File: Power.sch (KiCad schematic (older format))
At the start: 22 parts, among them U2 MCP1700T-3302E/TT_

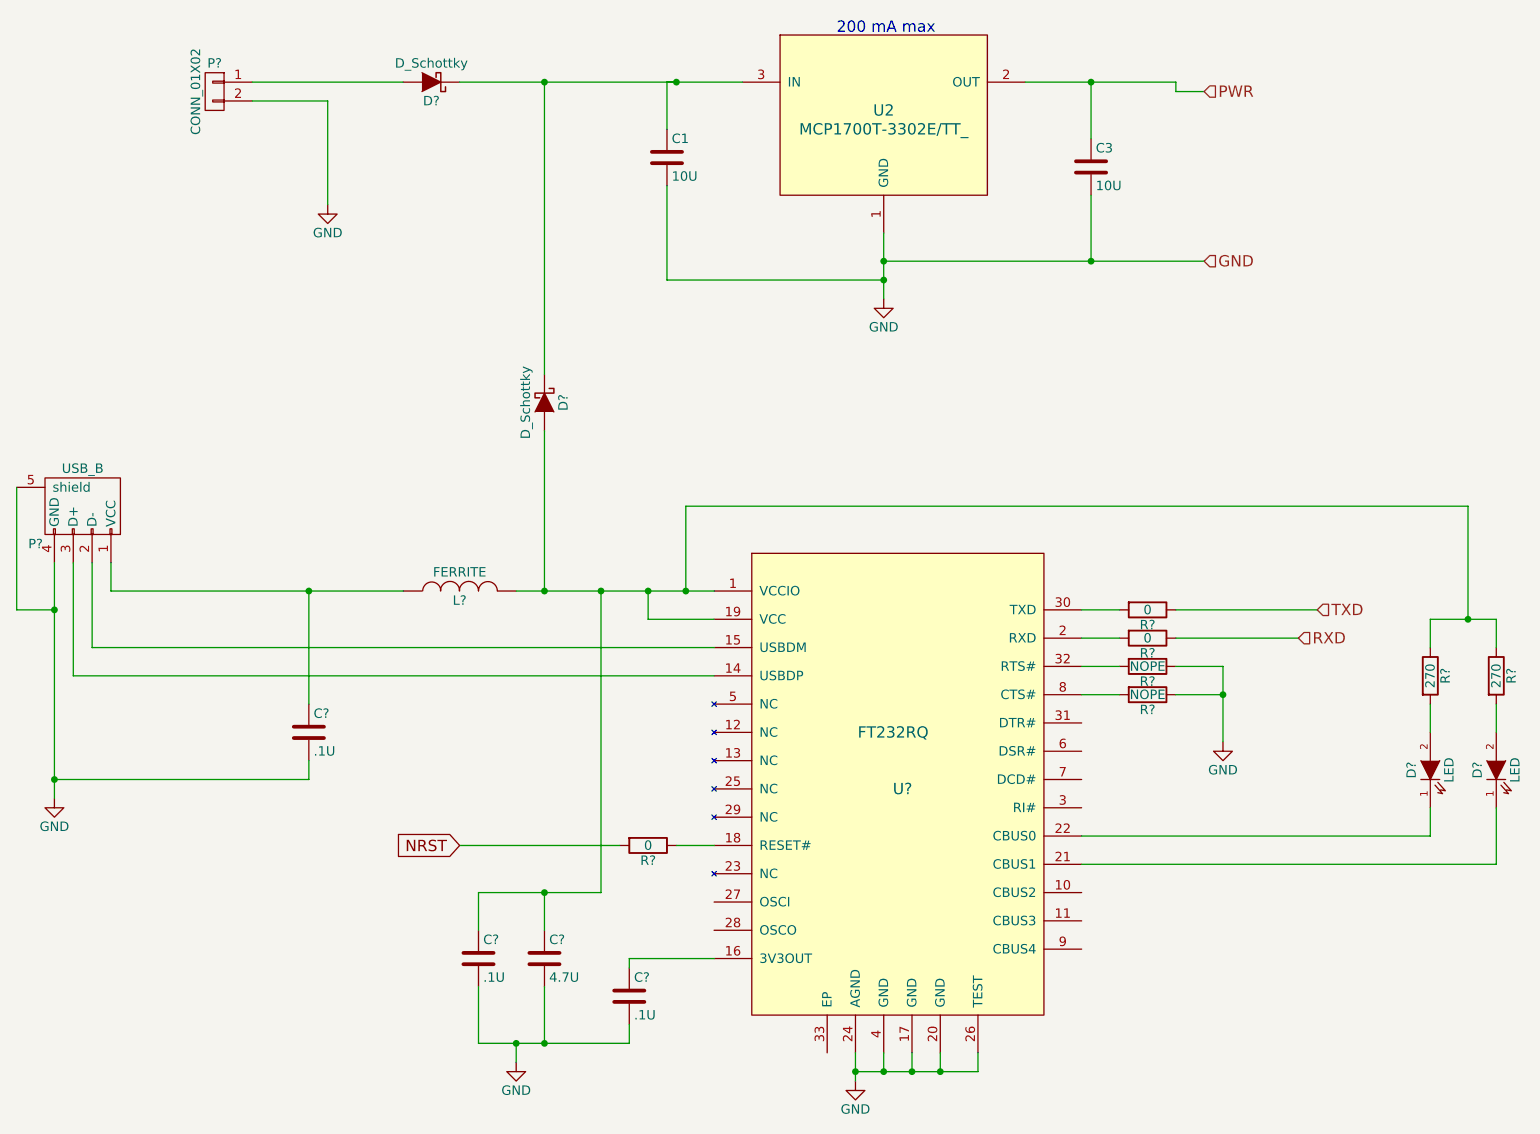
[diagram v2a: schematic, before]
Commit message: Associated footprints, created footprints for 2mm connector and did prelim placement
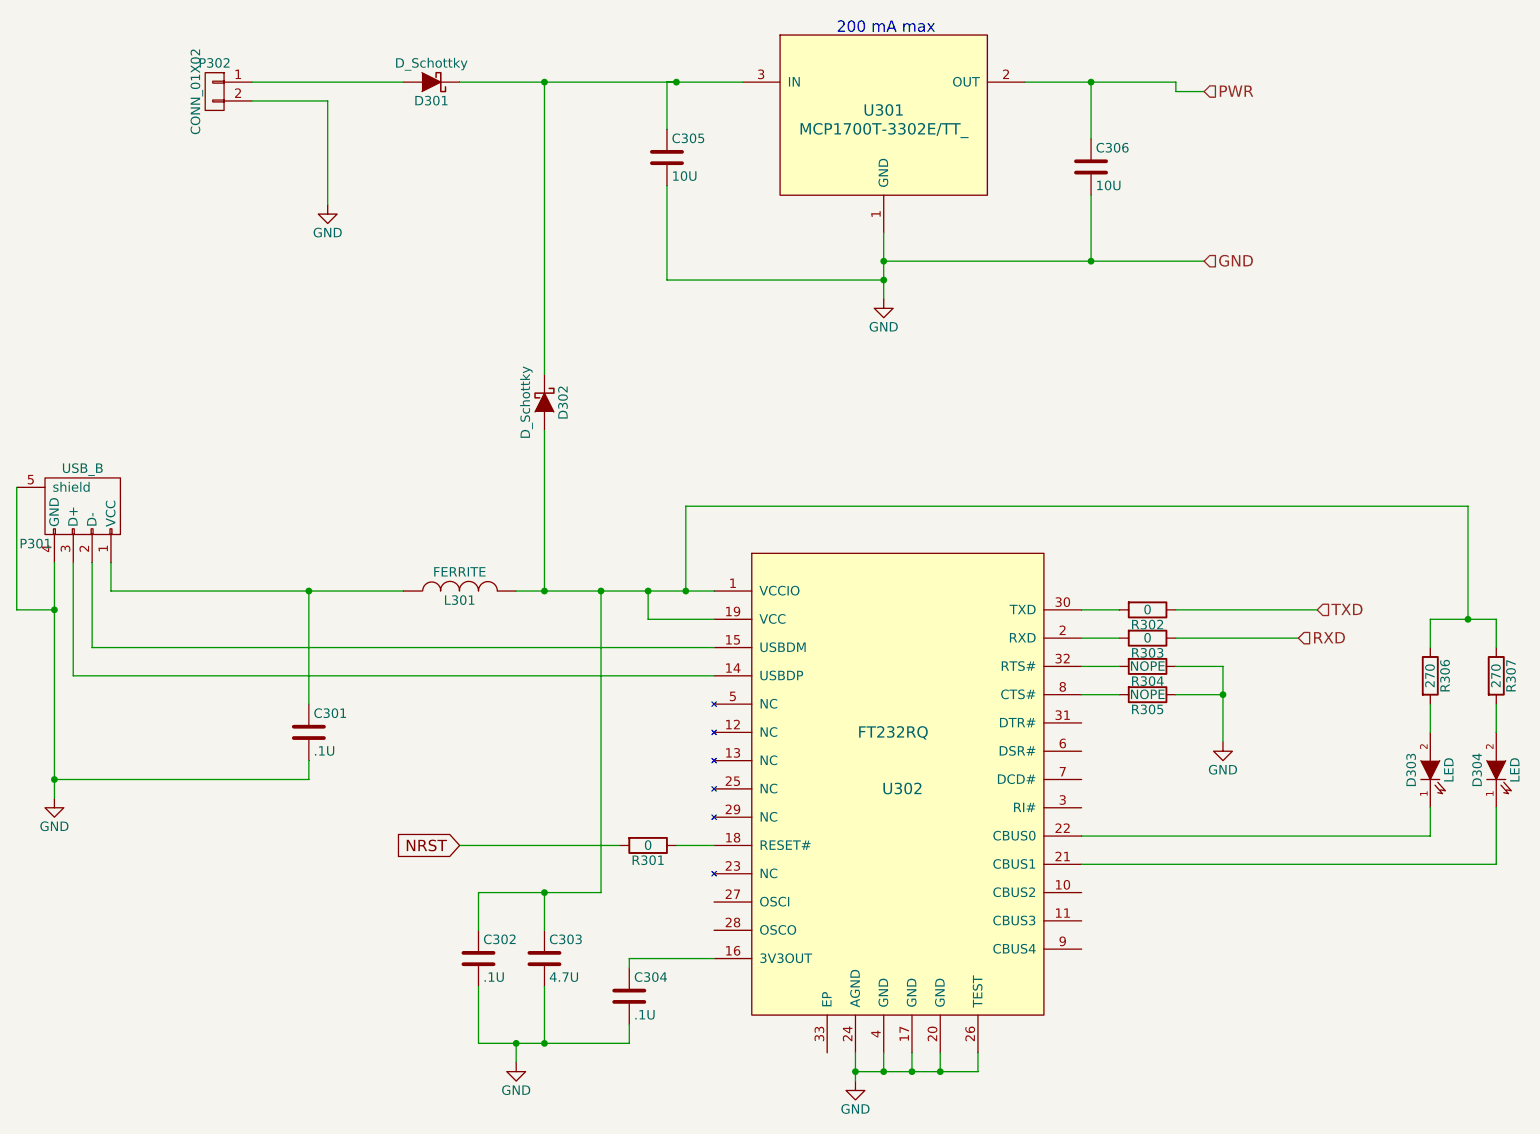
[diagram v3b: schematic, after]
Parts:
- C301, C302, C304: renamed from C?; footprint (none) -> Capacitors_SMD:C_0805
- C303: renamed from C?; footprint (none) -> Capacitors_SMD:C_1210
- C305: renamed from C1; footprint Capacitors_SMD:C_0805 -> Capacitors_SMD:C_1210
- C306: renamed from C3; footprint Capacitors_SMD:C_0805 -> Capacitors_SMD:C_1210
- D301, D302: renamed from D?; footprint (none) -> Diodes_SMD:Diode-SMA_Standard
- D303, D304: renamed from D?; footprint (none) -> LEDs:LED-0805
- L301: renamed from L?; footprint (none) -> Inductors_NEOSID:Neosid_Inductor_SM1206
- P301: renamed from P?; footprint (none) -> CentralCommand:10118193
- P302: renamed from P?; footprint (none) -> Pin_Headers:Pin_Header_Straight_1x02
- R301, R302, R303, R304, R305, R306, R307: renamed from R?; footprint (none) -> Resistors_SMD:R_0805
- U302: renamed from U?; footprint (none) -> Housings_DFN_QFN:QFN-32-1EP_5x5mm_Pitch0.5mm
- renumbered U2 to U301
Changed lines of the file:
@@
 $Descr A4 11693 8268
 encoding utf-8
-Sheet 2 3
+Sheet 3 3
 Title ""
 Date ""
@@
 $EndDescr
 $Comp
-L MCP1700T-3302E/TT_ U2
+L MCP1700T-3302E/TT_ U301
 U 1 1 56441A93
 P 5500 1100
-F 0 "U2" H 5500 1100 60  0000 C CNN
+F 0 "U301" H 5500 1100 60  0000 C CNN
 F 1 "MCP1700T-3302E/TT_" H 5500 1000 60  0000 C CNN
 F 2 "Housings_SOT-23_SOT-143_TSOT-6:SOT-23" H 5500 1100 60  0001 C CNN
@@
 $EndComp
 $Comp
-L C C1
+L C C305
 U 1 1 56441A9A
 P 4350 1350
-F 0 "C1" H 4375 1450 50  0000 L CNN
+F 0 "C305" H 4375 1450 50  0000 L CNN
 F 1 "10U" H 4375 1250 50  0000 L CNN
-F 2 "Capacitors_SMD:C_0805" H 4388 1200 30  0001 C CNN
+F 2 "Capacitors_SMD:C_1210" H 4388 1200 30  0001 C CNN
 F 3 "" H 4350 1350 60  0000 C CNN
 	1    4350 1350
@@
 $EndComp
 $Comp
-L C C3
+L C C306
 U 1 1 56441AA1
 P 6600 1400
-F 0 "C3" H 6625 1500 50  0000 L CNN
+F 0 "C306" H 6625 1500 50  0000 L CNN
 F 1 "10U" H 6625 1300 50  0000 L CNN
-F 2 "Capacitors_SMD:C_0805" H 6638 1250 30  0001 C CNN
+F 2 "Capacitors_SMD:C_1210" H 6638 1250 30  0001 C CNN
 F 3 "" H 6600 1400 60  0000 C CNN
 	1    6600 1400
@@
 $EndComp
 $Comp
-L GND #PWR?
+L GND #PWR08
 U 1 1 56441AA8
 P 5500 2100
-F 0 "#PWR?" H 5500 1850 50  0001 C CNN
+F 0 "#PWR08" H 5500 1850 50  0001 C CNN
 F 1 "GND" H 5500 1950 50  0000 C CNN
 F 2 "" H 5500 2100 60  0000 C CNN
@@
 200 mA max
 $Comp
-L CONN_01X02 P?
+L CONN_01X02 P302
 U 1 1 56442D62
 P 1950 1000
-F 0 "P?" H 1950 1150 50  0000 C CNN
+F 0 "P302" H 1950 1150 50  0000 C CNN
 F 1 "CONN_01X02" V 2050 1000 50  0000 C CNN
-F 2 "" H 1950 1000 60  0000 C CNN
+F 2 "Pin_Headers:Pin_Header_Straight_1x02" H 1950 1000 60  0001 C CNN
 F 3 "" H 1950 1000 60  0000 C CNN
 	1    1950 1000
@@
 $EndComp
 $Comp
-L GND #PWR?
+L GND #PWR09
 U 1 1 56442E32
 P 2550 1600
-F 0 "#PWR?" H 2550 1350 50  0001 C CNN
+F 0 "#PWR09" H 2550 1350 50  0001 C CNN
 F 1 "GND" H 2550 1450 50  0000 C CNN
 F 2 "" H 2550 1600 60  0000 C CNN
@@
 $EndComp
 $Comp
-L FT232RQ U?
+L FT232RQ U302
 U 1 1 565601D9
 P 5550 4750
-F 0 "U?" H 5600 4800 60  0000 C CNN
+F 0 "U302" H 5600 4800 60  0000 C CNN
 F 1 "FT232RQ" H 5550 5100 60  0000 C CNN
-F 2 "" H 7700 4900 60  0000 C CNN
+F 2 "Housings_DFN_QFN:QFN-32-1EP_5x5mm_Pitch0.5mm" H 7700 4900 60  0001 C CNN
 F 3 "" H 7700 4900 60  0000 C CNN
 	1    5550 4750
@@
 $EndComp
 $Comp
-L USB_B P?
+L USB_B P301
 U 1 1 56560CE5
 P 1200 3200
-F 0 "P?" H 1400 3000 50  0000 C CNN
+F 0 "P301" H 1400 3000 50  0000 C CNN
 F 1 "USB_B" H 1150 3400 50  0000 C CNN
-F 2 "" V 1150 3100 60  0000 C CNN
+F 2 "CentralCommand:10118193" V 1150 3100 60  0001 C CNN
 F 3 "" V 1150 3100 60  0000 C CNN
 	1    1200 3200
@@
 	2550 1050 2550 1600
 $Comp
-L INDUCTOR L?
+L INDUCTOR L301
 U 1 1 56560EFA
 P 3250 3650
-F 0 "L?" V 3200 3650 50  0000 C CNN
+F 0 "L301" V 3200 3650 50  0000 C CNN
 F 1 "FERRITE" V 3350 3650 50  0000 C CNN
-F 2 "" H 3250 3650 60  0000 C CNN
+F 2 "Inductors_NEOSID:Neosid_Inductor_SM1206" H 3250 3650 60  0001 C CNN
 F 3 "" H 3250 3650 60  0000 C CNN
 	1    3250 3650
@@
 	1400 3650 2950 3650
 $Comp
-L C C?
+L C C301
 U 1 1 565612DF
 P 2450 4400
-F 0 "C?" H 2475 4500 50  0000 L CNN
+F 0 "C301" H 2475 4500 50  0000 L CNN
 F 1 ".1U" H 2475 4300 50  0000 L CNN
-F 2 "" H 2488 4250 30  0000 C CNN
+F 2 "Capacitors_SMD:C_0805" H 2488 4250 30  0001 C CNN
 F 3 "" H 2450 4400 60  0000 C CNN
 	1    2450 4400
@@
 	1100 3500 1100 4750
 $Comp
-L GND #PWR?
+L GND #PWR010
 U 1 1 565615CA
 P 1100 4750
-F 0 "#PWR?" H 1100 4500 50  0001 C CNN
+F 0 "#PWR010" H 1100 4500 50  0001 C CNN
 F 1 "GND" H 1100 4600 50  0000 C CNN
 F 2 "" H 1100 4750 60  0000 C CNN
@@
 RXD
 $Comp
-L D_Schottky D?
+L D_Schottky D301
 U 1 1 565622B8
 P 3100 950
-F 0 "D?" H 3100 1050 50  0000 C CNN
+F 0 "D301" H 3100 1050 50  0000 C CNN
 F 1 "D_Schottky" H 3100 850 50  0000 C CNN
-F 2 "" H 3100 950 60  0000 C CNN
+F 2 "Diodes_SMD:Diode-SMA_Standard" H 3100 950 60  0001 C CNN
 F 3 "" H 3100 950 60  0000 C CNN
 	1    3100 950
@@
 	2950 950  2150 950
 $Comp
-L D_Schottky D?
+L D_Schottky D302
 U 1 1 565637EA
 P 3700 2650
-F 0 "D?" H 3700 2750 50  0000 C CNN
+F 0 "D302" H 3700 2750 50  0000 C CNN
 F 1 "D_Schottky" H 3700 2550 50  0000 C CNN
-F 2 "" H 3700 2650 60  0000 C CNN
+F 2 "Diodes_SMD:Diode-SMA_Standard" H 3700 2650 60  0001 C CNN
 F 3 "" H 3700 2650 60  0000 C CNN
 	1    3700 2650
@@
 PWR
 $Comp
-L C C?
+L C C303
 U 1 1 56567F6F
 P 3700 5600
-F 0 "C?" H 3725 5700 50  0000 L CNN
+F 0 "C303" H 3725 5700 50  0000 L CNN
 F 1 "4.7U" H 3725 5500 50  0000 L CNN
-F 2 "" H 3738 5450 30  0000 C CNN
+F 2 "Capacitors_SMD:C_1210" H 3738 5450 30  0001 C CNN
 F 3 "" H 3700 5600 60  0000 C CNN
 	1    3700 5600
@@
 $EndComp
 $Comp
-L C C?
+L C C302
 U 1 1 56567FCE
 P 3350 5600
-F 0 "C?" H 3375 5700 50  0000 L CNN
+F 0 "C302" H 3375 5700 50  0000 L CNN
 F 1 ".1U" H 3375 5500 50  0000 L CNN
-F 2 "" H 3388 5450 30  0000 C CNN
+F 2 "Capacitors_SMD:C_0805" H 3388 5450 30  0001 C CNN
 F 3 "" H 3350 5600 60  0000 C CNN
 	1    3350 5600
@@
 	3350 6050 3350 5750
 $Comp
-L GND #PWR?
+L GND #PWR011
 U 1 1 56568175
 P 3550 6150
-F 0 "#PWR?" H 3550 5900 50  0001 C CNN
+F 0 "#PWR011" H 3550 5900 50  0001 C CNN
 F 1 "GND" H 3550 6000 50  0000 C CNN
 F 2 "" H 3550 6150 60  0000 C CNN
@@
 Connection ~ 3550 6050
 $Comp
-L C C?
+L C C304
 U 1 1 565684E2
 P 4150 5800
-F 0 "C?" H 4175 5900 50  0000 L CNN
+F 0 "C304" H 4175 5900 50  0000 L CNN
 F 1 ".1U" H 4175 5700 50  0000 L CNN
-F 2 "" H 4188 5650 30  0000 C CNN
+F 2 "Capacitors_SMD:C_0805" H 4188 5650 30  0001 C CNN
 F 3 "" H 4150 5800 60  0000 C CNN
 	1    4150 5800
@@
 	3250 5000 4100 5000
 $Comp
-L R R?
+L R R301
 U 1 1 565699C8
 P 4250 5000
-F 0 "R?" V 4330 5000 50  0000 C CNN
+F 0 "R301" V 4330 5000 50  0000 C CNN
 F 1 "0" V 4250 5000 50  0000 C CNN
-F 2 "" V 4180 5000 30  0000 C CNN
+F 2 "Resistors_SMD:R_0805" V 4180 5000 30  0001 C CNN
 F 3 "" H 4250 5000 30  0000 C CNN
 	1    4250 5000
@@
 	4400 5000 4600 5000
 $Comp
-L GND #PWR?
+L GND #PWR012
 U 1 1 5656A044
 P 5350 6250
-F 0 "#PWR?" H 5350 6000 50  0001 C CNN
+F 0 "#PWR012" H 5350 6000 50  0001 C CNN
 F 1 "GND" H 5350 6100 50  0000 C CNN
 F 2 "" H 5350 6250 60  0000 C CNN
@@
 Connection ~ 5500 6200
 $Comp
-L R R?
+L R R306
 U 1 1 5656BA48
 P 8400 4100
-F 0 "R?" V 8480 4100 50  0000 C CNN
+F 0 "R306" V 8480 4100 50  0000 C CNN
 F 1 "270" V 8400 4100 50  0000 C CNN
-F 2 "" V 8330 4100 30  0000 C CNN
+F 2 "Resistors_SMD:R_0805" V 8330 4100 30  0001 C CNN
 F 3 "" H 8400 4100 30  0000 C CNN
 	1    8400 4100
@@
 $EndComp
 $Comp
-L LED D?
+L LED D303
 U 1 1 5656BA7D
 P 8400 4600
-F 0 "D?" H 8400 4700 50  0000 C CNN
+F 0 "D303" H 8400 4700 50  0000 C CNN
 F 1 "LED" H 8400 4500 50  0000 C CNN
-F 2 "" H 8400 4600 60  0000 C CNN
+F 2 "LEDs:LED-0805" H 8400 4600 60  0001 C CNN
 F 3 "" H 8400 4600 60  0000 C CNN
 	1    8400 4600
@@
 $EndComp
 $Comp
-L R R?
+L R R307
 U 1 1 5656BBCB
 P 8750 4100
-F 0 "R?" V 8830 4100 50  0000 C CNN
+F 0 "R307" V 8830 4100 50  0000 C CNN
 F 1 "270" V 8750 4100 50  0000 C CNN
-F 2 "" V 8680 4100 30  0000 C CNN
+F 2 "Resistors_SMD:R_0805" V 8680 4100 30  0001 C CNN
 F 3 "" H 8750 4100 30  0000 C CNN
 	1    8750 4100
@@
 $EndComp
 $Comp
-L LED D?
+L LED D304
 U 1 1 5656BBD1
 P 8750 4600
-F 0 "D?" H 8750 4700 50  0000 C CNN
+F 0 "D304" H 8750 4700 50  0000 C CNN
 F 1 "LED" H 8750 4500 50  0000 C CNN
-F 2 "" H 8750 4600 60  0000 C CNN
+F 2 "LEDs:LED-0805" H 8750 4600 60  0001 C CNN
 F 3 "" H 8750 4600 60  0000 C CNN
 	1    8750 4600
@@
 Connection ~ 4450 3650
 $Comp
-L R R?
+L R R304
 U 1 1 5656CCE7
 P 6900 4050
-F 0 "R?" V 6980 4050 50  0000 C CNN
+F 0 "R304" V 6980 4050 50  0000 C CNN
 F 1 "NOPE" V 6900 4050 50  0000 C CNN
-F 2 "" V 6830 4050 30  0000 C CNN
+F 2 "Resistors_SMD:R_0805" V 6830 4050 30  0001 C CNN
 F 3 "" H 6900 4050 30  0000 C CNN
 	1    6900 4050
@@
 $EndComp
 $Comp
-L R R?
+L R R305
 U 1 1 5656CE8C
 P 6900 4200
-F 0 "R?" V 6980 4200 50  0000 C CNN
+F 0 "R305" V 6980 4200 50  0000 C CNN
 F 1 "NOPE" V 6900 4200 50  0000 C CNN
-F 2 "" V 6830 4200 30  0000 C CNN
+F 2 "Resistors_SMD:R_0805" V 6830 4200 30  0001 C CNN
 F 3 "" H 6900 4200 30  0000 C CNN
 	1    6900 4200
@@
 Connection ~ 7300 4200
 $Comp
-L GND #PWR?
+L GND #PWR013
 U 1 1 5656D2A7
 P 7300 4450
-F 0 "#PWR?" H 7300 4200 50  0001 C CNN
+F 0 "#PWR013" H 7300 4200 50  0001 C CNN
 F 1 "GND" H 7300 4300 50  0000 C CNN
 F 2 "" H 7300 4450 60  0000 C CNN
@@
 Connection ~ 5800 6200
 $Comp
-L R R?
+L R R302
 U 1 1 5656E5CA
 P 6900 3750
-F 0 "R?" V 6980 3750 50  0000 C CNN
+F 0 "R302" V 6980 3750 50  0000 C CNN
 F 1 "0" V 6900 3750 50  0000 C CNN
-F 2 "" V 6830 3750 30  0000 C CNN
+F 2 "Resistors_SMD:R_0805" V 6830 3750 30  0001 C CNN
 F 3 "" H 6900 3750 30  0000 C CNN
 	1    6900 3750
@@
 $EndComp
 $Comp
-L R R?
+L R R303
 U 1 1 5656E668
 P 6900 3900
-F 0 "R?" V 6980 3900 50  0000 C CNN
+F 0 "R303" V 6980 3900 50  0000 C CNN
 F 1 "0" V 6900 3900 50  0000 C CNN
-F 2 "" V 6830 3900 30  0000 C CNN
+F 2 "Resistors_SMD:R_0805" V 6830 3900 30  0001 C CNN
 F 3 "" H 6900 3900 30  0000 C CNN
 	1    6900 3900
